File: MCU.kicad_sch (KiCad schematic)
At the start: 61 parts, among them J1 B6B-PH-SM4-TB, J2 5033981892, J3 B2B-PH-K-S, Q3 MBT3904DW1, Q4 BSS138, Q5 PDTC114EU_115, Q6 PDTC114EU_115, Q7 PDTC114EU_115, U10 TPL5010, U11 NL-SW-LTE-TC4NAG-B, U12 74AHC1G08, U9 ESP32-S3-WROOM-1-N16R8

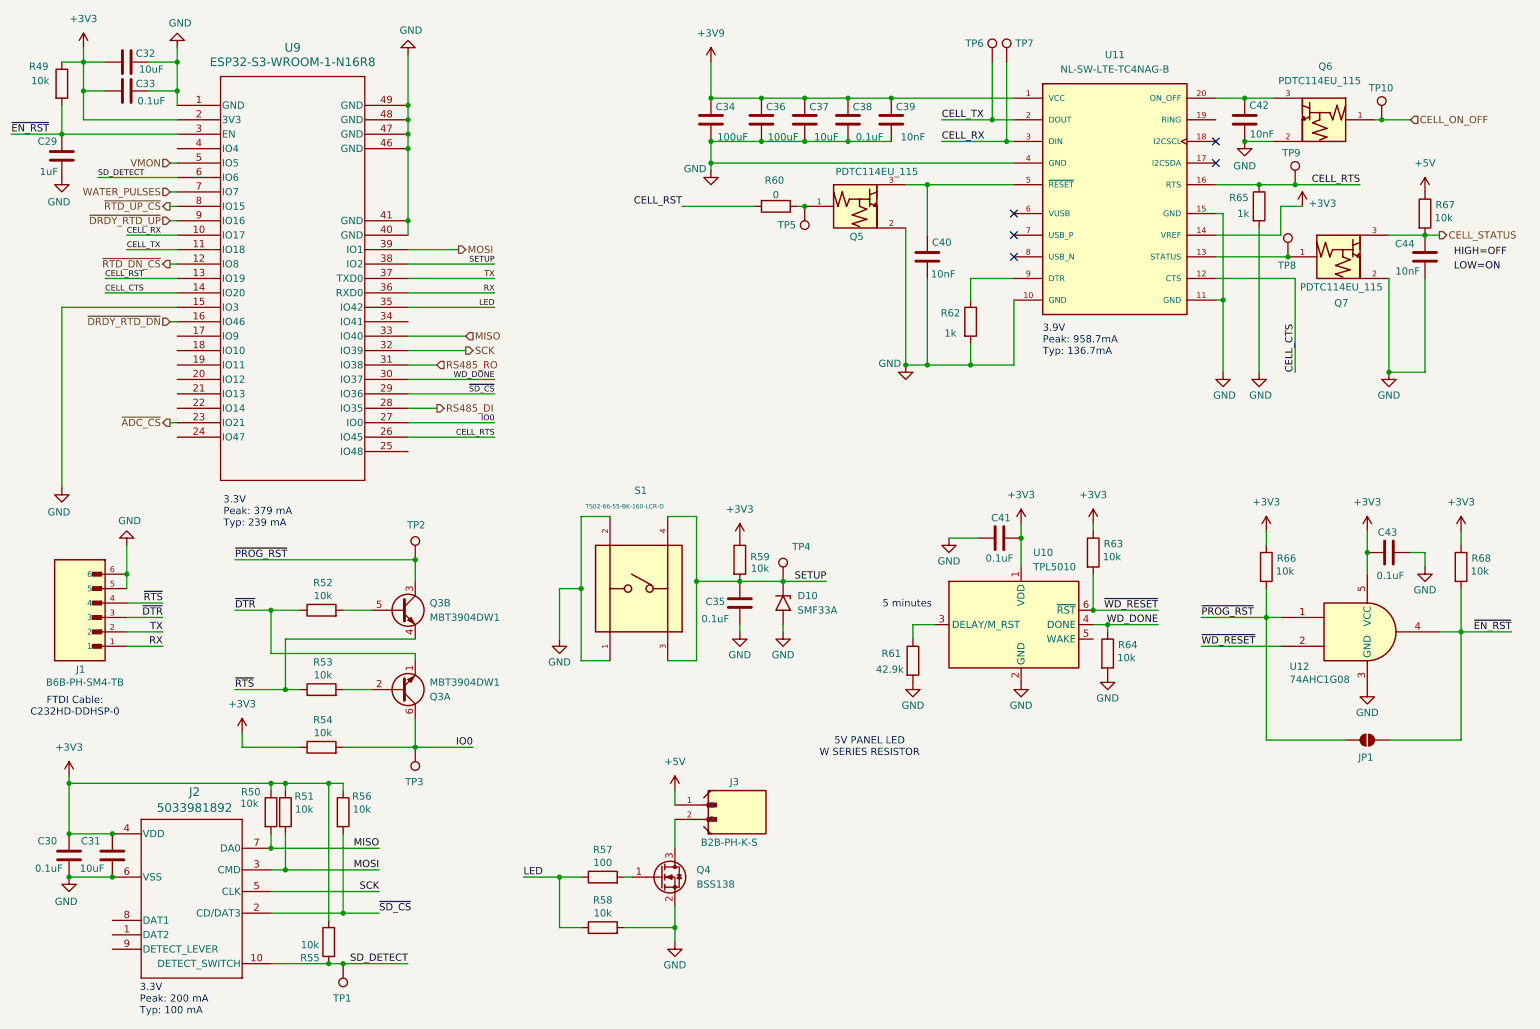
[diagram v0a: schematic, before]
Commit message: updated poe schematic
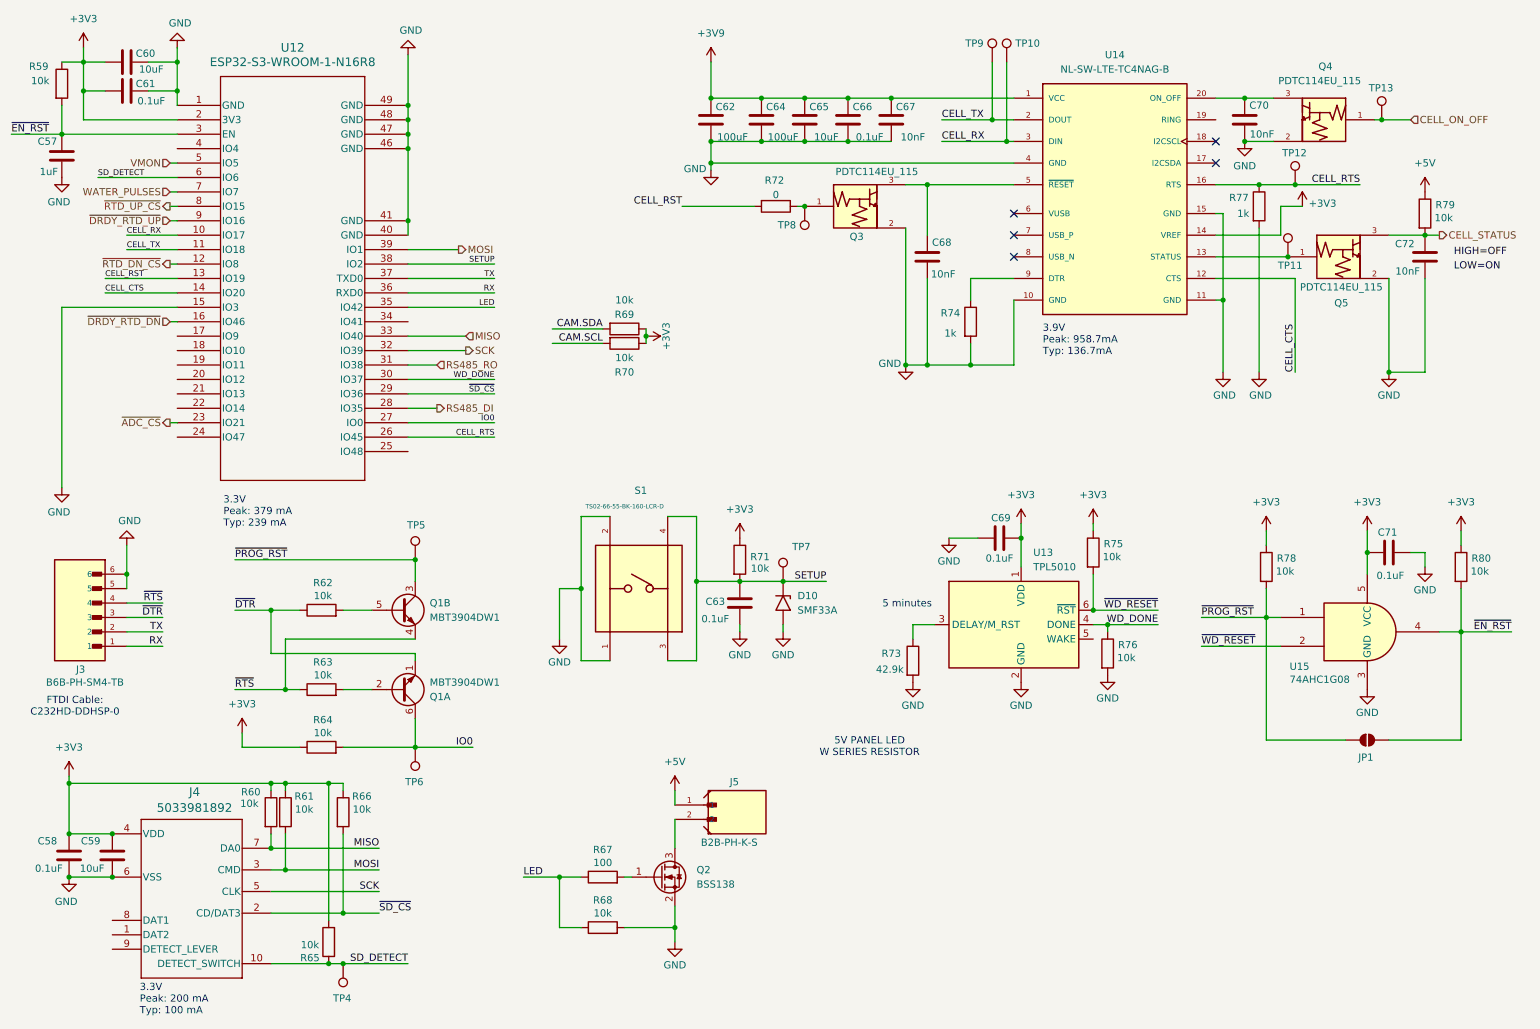
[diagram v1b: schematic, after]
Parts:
- added R69, R70: 10k_0402_0402WGF1002TCE, Resistor_SMD:R_0402_1005Metric, symbol 00-kiml-resistors-smd:10k_0402_0402WGF1002TCE
- renumbered C29 to C57, C30 to C58, C31 to C59, C32 to C60, C33 to C61, C34 to C62, C35 to C63, C36 to C64, C37 to C65, C38 to C66, C39 to C67, C40 to C68, C41 to C69, C42 to C70, C43 to C71, C44 to C72, J1 to J3, J2 to J4, J3 to J5, Q3 to Q1, Q4 to Q2, Q5 to Q3, Q6 to Q4, Q7 to Q5, R49 to R59, R50 to R60, R51 to R61, R52 to R62, R53 to R63, R54 to R64, R55 to R65, R56 to R66, R57 to R67, R58 to R68, R59 to R71, R60 to R72, R61 to R73, R62 to R74, R63 to R75, R64 to R76, R65 to R77, R66 to R78, R67 to R79, R68 to R80, TP7 to TP10, TP8 to TP11, TP9 to TP12, TP10 to TP13, TP1 to TP4, TP2 to TP5, TP3 to TP6, TP4 to TP7, TP5 to TP8, TP6 to TP9, U9 to U12, U10 to U13, U11 to U14, U12 to U15
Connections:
- net +3V3: now also R69.1, R70.1
- new net CAM.SCL: R70.2
- new net CAM.SDA: R69.2

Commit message: GPIOs shouldn't have any conflicts
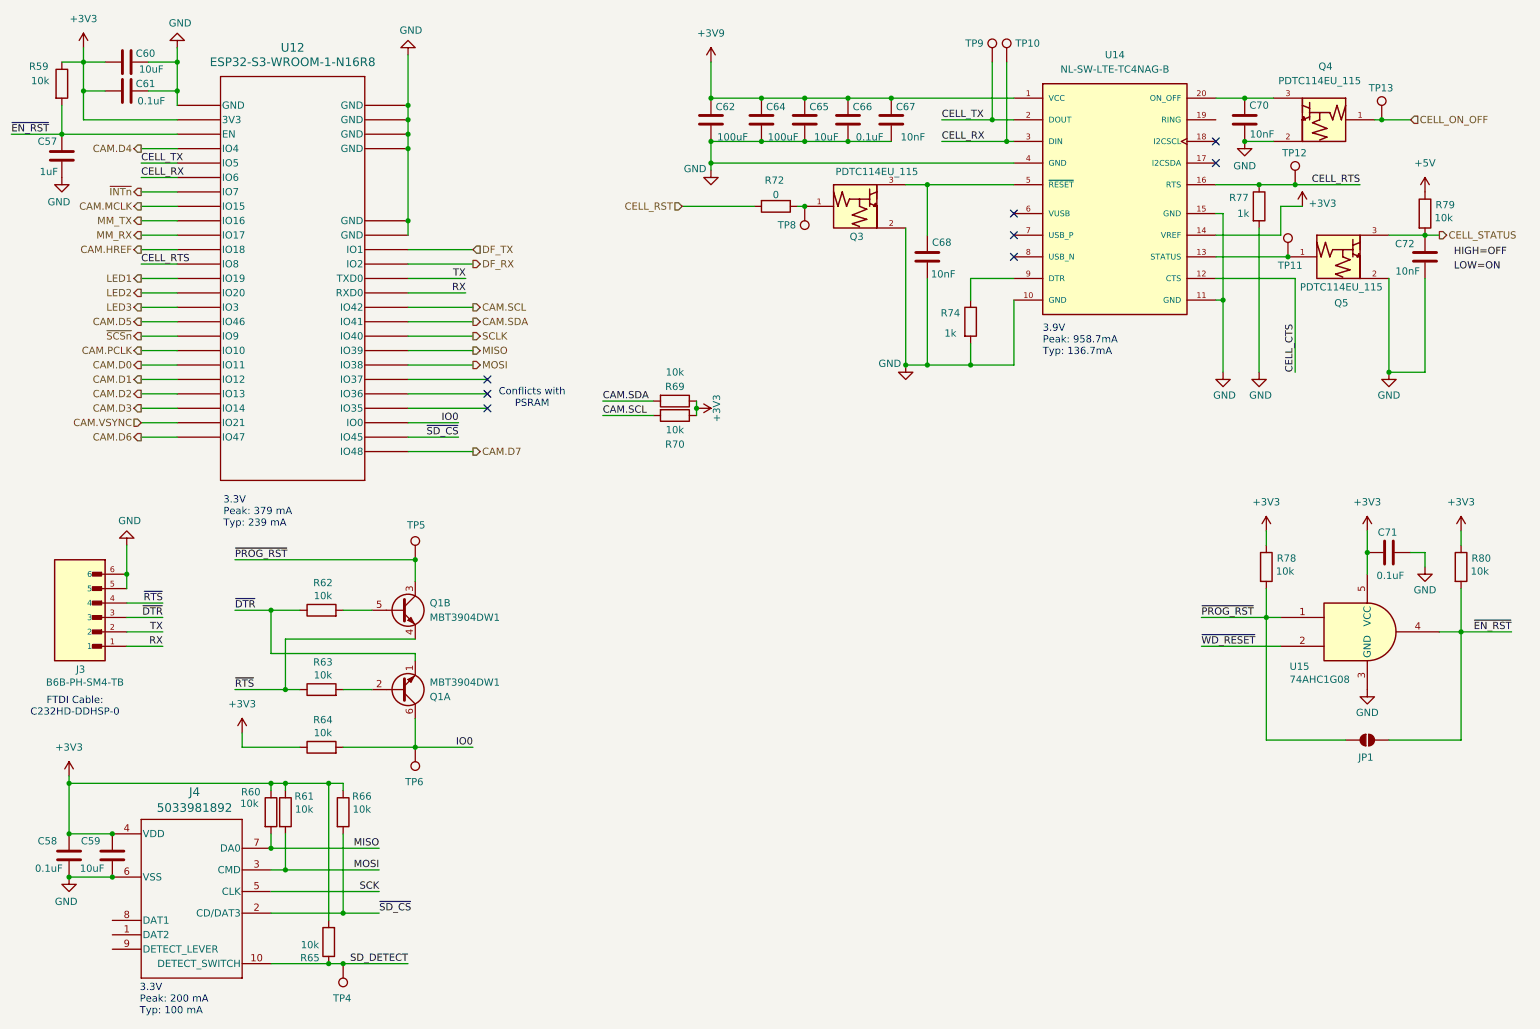
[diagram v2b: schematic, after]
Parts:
- removed C63, C69: 0.1uF, Capacitor_SMD:C_0603_1608Metric, symbol Device:C
- removed D10: SMF33A, Diode_SMD:D_SMF, symbol Diode:SMF33A
- removed J5: B2B-PH-K-S, B2B-PH-K-S:JST_B2B-PH-K-S, symbol B2B-PH-K-S:B2B-PH-K-S
- removed Q2: BSS138, Package_TO_SOT_SMD:SOT-23, symbol Transistor_FET:BSS138
- removed R67: 100, Resistor_SMD:R_0603_1608Metric, symbol Device:R
- removed R68, R71, R75, R76: 10k, Resistor_SMD:R_0603_1608Metric, symbol Device:R
- removed R73: 42.9k, Resistor_SMD:R_0603_1608Metric, symbol Device:R
- removed S1: TS02-66-55-BK-160-LCR-D, TS02-66-55-BK-160-LCR-D:SW_TS02-66-55-BK-160-LCR-D, symbol TS02-66-55-BK-160-LCR-D:TS02-66-55-BK-160-LCR-D
- removed TP7: TestPoint, TestPoint:TestPoint_Pad_D2.0mm, symbol Connector:TestPoint
- removed U13: TPL5010, Package_TO_SOT_SMD:SOT-23-6, symbol Timer:TPL5010
- U12: footprint ESP32-S3-WROOM-1_EXP -> ESP32-S3-WROOM-1-N16R8:ESP32-S3-WROOM-1_EXP
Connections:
- net LED is gone; now on net CAM.SCL: U12.35 (IO42)
- net RS485_RO is gone; now on net MOSI: U12.31 (IO38)
- net VMON is gone; now on net CELL_TX: U12.5 (IO5)
- net ~{RTD_DN_CS} is gone; now on net CELL_RTS: U12.12 (IO8)
- net CAM.SDA: now also U12.34 (IO41)
- net CELL_CTS: no longer U12.14 (IO20)
- net CELL_RST: no longer U12.13 (IO19)
- net CELL_RTS: no longer U12.26 (IO45)
- net CELL_RX: now also U12.6 (IO6); no longer U12.10 (IO17)
- net CELL_TX: no longer U12.11 (IO18)
- net GND: no longer U12.15 (IO3)
- net MISO: now also U12.32 (IO39); no longer U12.33 (IO40)
- net MOSI: no longer U12.39 (IO1)
- net SCK: no longer U12.32 (IO39)
- net SD_DETECT: no longer U12.6 (IO6)
- net ~{SD_CS}: now also U12.26 (IO45); no longer U12.29 (IO36)
- net ~{SCSn}: now reaches U12.17 (IO9)
- net CAM.PCLK: now reaches U12.18 (IO10)
- net CAM.D0: now reaches U12.19 (IO11)
- net CAM.D1: now reaches U12.20 (IO12)
- net CAM.D2: now reaches U12.21 (IO13)
- net CAM.D3: now reaches U12.22 (IO14)
- net CAM.D6: now reaches U12.24 (IO47)
- net CAM.D7: now reaches U12.25 (IO48)
- net CAM.D4: now reaches U12.4 (IO4)
- net RS485_DI: no longer names the net of U12.28 (IO35)
- net SETUP renamed DF_RX
- net WATER_PULSES renamed ~{INTn}
- net WD_DONE: no longer names the net of U12.30 (IO37)
- net ~{ADC_CS} renamed CAM.VSYNC
- net ~{DRDY_RTD_DN} renamed CAM.D5
- net ~{DRDY_RTD_UP} renamed MM_TX
- net ~{RTD_UP_CS} renamed CAM.MCLK
- new net CAM.HREF: U12.11 (IO18)
- new net DF_TX: U12.39 (IO1)
- new net LED1: U12.13 (IO19)
- new net LED2: U12.14 (IO20)
- new net LED3: U12.15 (IO3)
- new net MM_RX: U12.10 (IO17)
- new net SCLK: U12.33 (IO40)
- no-connect marks 5 -> 8
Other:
- note added: "Conflicts with PSRAM"
- note removed: "5 minutes"
- note removed: "5V PANEL LED W SERIES RESISTOR"
- moved on the sheet: R69, R70

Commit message: put all the components on the pcb on traces
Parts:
- removed C58: 0.1uF, Capacitor_SMD:C_0603_1608Metric, symbol Device:C
- removed C59: 10uF, Capacitor_SMD:C_0805_2012Metric, symbol Device:C
- removed J4: 5033981892, 5033981892:CONN_503398-1892_MOL, symbol 5033981892:5033981892
- removed R60, R61, R65, R66: 10k, Resistor_SMD:R_0603_1608Metric, symbol Device:R
- removed TP4: TestPoint, TestPoint:TestPoint_Pad_D2.0mm, symbol Connector:TestPoint
- added C20, C24: 0.1uF, Capacitor_SMD:C_0603_1608Metric, symbol Device:C
- added D10: SMF33A, Diode_SMD:D_SMF, symbol Diode:SMF33A
- added J5: B2B-PH-K-S, B2B-PH-K-S:JST_B2B-PH-K-S, symbol B2B-PH-K-S:B2B-PH-K-S
- added J9: 878980204, 87898-0204:87898-0204_MOL, symbol 87898-0204:878980204
- added Q2: BSS138, Package_TO_SOT_SMD:SOT-23, symbol Transistor_FET:BSS138
- added R22, R23, R27, R28: 10k, Resistor_SMD:R_0603_1608Metric, symbol Device:R
- added R24: 42.9k, Resistor_SMD:R_0603_1608Metric, symbol Device:R
- added R67: 100, Resistor_SMD:R_0603_1608Metric, symbol Device:R
- added S1: TS02-66-55-BK-160-LCR-D, TS02-66-55-BK-160-LCR-D:SW_TS02-66-55-BK-160-LCR-D, symbol TS02-66-55-BK-160-LCR-D:TS02-66-55-BK-160-LCR-D
- added TP7: TestPoint, TestPoint:TestPoint_Pad_D2.0mm, symbol Connector:TestPoint
- added U13: TPL5010, Package_TO_SOT_SMD:SOT-23-6, symbol Timer:TPL5010
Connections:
- net CAM.D3 is gone; now on net CELL_RTS: U12.22 (IO14)
- net CAM.HREF is gone; now on net CELL_RX: U12.11 (IO18)
- net CAM.MCLK is gone; now on net CELL_CTS: U12.8 (IO15)
- net CAM.VSYNC is gone; now on net DF_RX: U12.23 (IO21)
- net +3V3: now also C24.2, R23.1, R27.1, U13.1 (VDD)
- net +5V: now also J5.1
- net CELL_RTS: no longer U12.12 (IO8)
- net CELL_RX: no longer U12.6 (IO6)
- net CELL_TX: now also U12.10 (IO17); no longer U12.5 (IO5)
- net DF_RX: no longer U12.38 (IO2)
- net DF_TX: now also U12.9 (IO16); no longer U12.39 (IO1)
- net GND: now also C20.2, C24.1, D10.2 (A2), Q2.2 (S), R22.2, R24.2, R28.2, S1.1, S1.2, U13.2 (GND)
- net LED1: now also U12.15 (IO3); no longer U12.13 (IO19)
- net LED2: now also U12.5 (IO5); no longer U12.14 (IO20)
- net LED3: now also U12.6 (IO6); no longer U12.15 (IO3)
- net MM_RX: now also U12.39 (IO1); no longer U12.10 (IO17)
- net MM_TX: now also U12.38 (IO2); no longer U12.9 (IO16)
- net ~{SD_CS}: now also U12.35 (IO42); no longer U12.26 (IO45)
- net ~{WD_RESET}: now also R27.2, U13.6 (~{RST})
- net CAM.D0 renamed ETH_MOSI
- net CAM.D1 renamed ETH_SCLK
- net CAM.D2 renamed ETH_MISO
- net CAM.D4 renamed SETUP
- net SETUP: now also C20.1, D10.1 (A1), R23.2, S1.3, S1.4, TP7.1
- net CAM.D5 renamed LED
- net LED: now also R22.1, R67.1
- net CAM.D6 renamed SDA
- net SDA: now also R69.2
- net CAM.D7 renamed SCL
- net SCL: now also R70.2
- net CAM.PCLK renamed ETH_CS
- removed net CAM.SCL: R70.2, U12.35 (IO42)
- net CAM.SDA renamed ~{CAM_CS}
- net ~{CAM_CS}: no longer R69.2
- net MISO renamed CAM_SD_MOSI
- net MOSI renamed CAM_SD_CLK
- net SCLK renamed CAM_SD_MISO
- net ~{SCSn} renamed MM_RTS
- new net: J5.2, Q2.3 (D)
- new net: R24.1, U13.3 (DELAY/M_RST)
- new net: Q2.1 (G), R67.2
- new net MM_CTS: U12.12 (IO8)
- new net USB+: J9.2, U12.14 (IO20)
- new net USB-: J9.1, U12.13 (IO19)
- new net WD_DONE: R28.1, U13.4 (DONE)
- new net ~{IO_RST}: U12.26 (IO45)
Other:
- note added: "5 minutes"
- note added: "5V PANEL LED W SERIES RESISTOR"
- note removed: "3.3V Peak: 200 mA Typ: 100 mA"

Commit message: wip - started traces for layout
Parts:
- removed J9: 878980204, 87898-0204:87898-0204_MOL, symbol 87898-0204:878980204
- removed TP5, TP6: TestPoint, TestPoint:TestPoint_Pad_D2.0mm, symbol Connector:TestPoint
- renumbered C57 to C45, C60 to C46, C61 to C47, C62 to C48, C20 to C49, C64 to C50, C65 to C51, C66 to C52, C67 to C53, C68 to C54, C24 to C55, C70 to C56, C71 to C57, C72 to C58, D10 to D7, J5 to J4, R59 to R43, R62 to R44, R63 to R45, R64 to R46, R67 to R47, R22 to R48, R69 to R49, R70 to R50, R23 to R51, R72 to R52, R24 to R53, R74 to R54, R27 to R55, R28 to R56, R77 to R57, R78 to R58, R79 to R59, R80 to R60, TP9 to TP10, TP10 to TP11, TP11 to TP12, TP12 to TP13, TP13 to TP14, TP7 to TP8, TP8 to TP9, U14 to U10, U15 to U11, U12 to U8, U13 to U9
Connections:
- net CAM_SD_CLK renamed CAM_SD_SCLK
- net ETH_CS renamed ~{ETH_CS}
- net USB+ renamed STROBE/USB+
- net USB- renamed BUZZ/USB-
- net ~{INTn} renamed ~{ETH_INT}
